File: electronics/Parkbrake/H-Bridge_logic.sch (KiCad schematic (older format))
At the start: 24 parts, among them U1 74LVC00, U2 74LVC08, U3 74LVC00, U4 74LVC08

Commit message: Spelling
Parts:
- U1, U3: farnell 2438786 -> 1105931; part 74LVC00APW.118 -> SN74LVC00APWR
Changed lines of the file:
@@
 F 2 "Housings_SSOP:TSSOP-14_4.4x5mm_Pitch0.65mm" H 1975 4775 50  0001 C CNN
 F 3 "" H 1975 4775 50  0000 C CNN
-F 4 "74LVC00APW.118" V 1975 4775 60  0001 C CNN "part"
-F 5 "2438786" V 1975 4775 60  0001 C CNN "farnell"
+F 4 "SN74LVC00APWR" V 1975 4775 60  0001 C CNN "part"
+F 5 "	1105931" V 1975 4775 60  0001 C CNN "farnell"
 	1    1975 4775
 	1    0    0    -1
@@
 F 2 "Housings_SSOP:TSSOP-14_4.4x5mm_Pitch0.65mm" H 6000 2025 50  0001 C CNN
 F 3 "" H 6000 2025 50  0000 C CNN
-F 4 "74LVC00APW.118" H 6000 2025 60  0001 C CNN "part"
-F 5 "2438786" H 6000 2025 60  0001 C CNN "farnell"
+F 4 "SN74LVC00APWR" H 6000 2025 60  0001 C CNN "part"
+F 5 "1105931" H 6000 2025 60  0001 C CNN "farnell"
 	1    6000 2025
 	1    0    0    -1

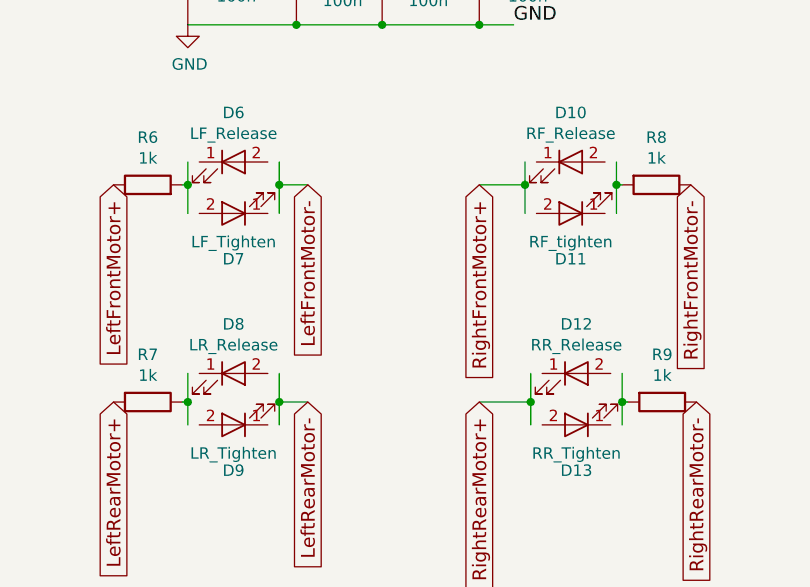
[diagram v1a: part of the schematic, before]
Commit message: minor tweaks to pcb, had a cap on wrong polarity
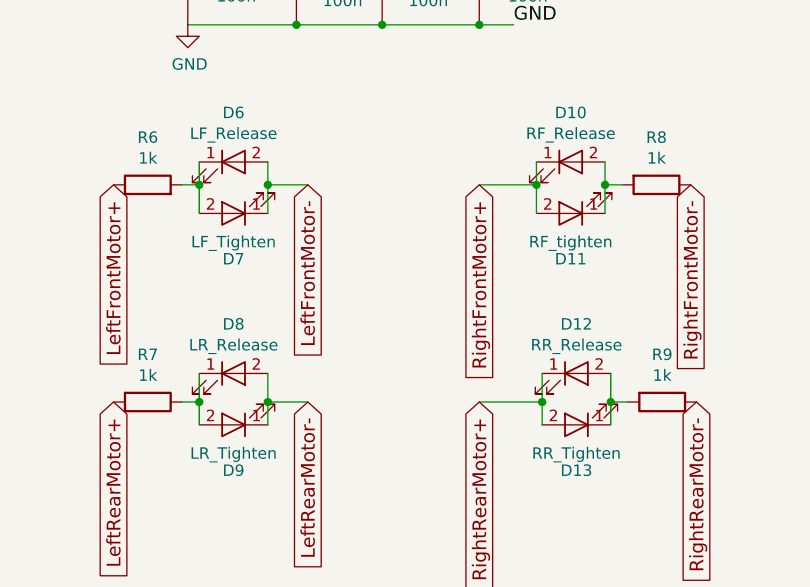
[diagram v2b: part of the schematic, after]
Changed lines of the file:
@@
 Connection ~ 2700 1200
-Wire Wire Line
-	3300 1800 3300 2025
-Wire Wire Line
-	3325 1900 3300 1900
-Connection ~ 3300 1900
-Wire Wire Line
-	2900 1800 2900 2025
-Wire Wire Line
-	2900 1900 2700 1900
-Connection ~ 2900 1900
-Wire Wire Line
-	1425 2725 1425 2950
-Wire Wire Line
-	1400 2850 1425 2850
-Connection ~ 1425 2850
-Wire Wire Line
-	1825 2725 1825 2950
-Wire Wire Line
-	1825 2850 1950 2850
-Connection ~ 1825 2850
-Wire Wire Line
-	1825 1800 1825 2025
-Wire Wire Line
-	1825 1900 1950 1900
-Connection ~ 1825 1900
-Wire Wire Line
-	1425 1800 1425 2025
-Wire Wire Line
-	1425 1900 1400 1900
-Connection ~ 1425 1900
-Wire Wire Line
-	3325 2725 3325 2950
-Wire Wire Line
-	3350 2850 3325 2850
-Connection ~ 3325 2850
-Wire Wire Line
-	2925 2725 2925 2950
-Wire Wire Line
-	2925 2850 2700 2850
-Connection ~ 2925 2850
 Wire Wire Line
 	2575 4775 2575 5175
@@
 	1    0    0    -1
 $EndComp
+Wire Wire Line
+	1775 1800 1775 2025
+Wire Wire Line
+	1475 1800 1475 2025
+Wire Wire Line
+	1400 1900 1475 1900
+Connection ~ 1475 1900
+Wire Wire Line
+	2950 1800 2950 2025
+Wire Wire Line
+	2700 1900 2950 1900
+Connection ~ 2950 1900
+Wire Wire Line
+	3250 1800 3250 2025
+Wire Wire Line
+	3325 1900 3250 1900
+Connection ~ 3250 1900
+Wire Wire Line
+	2975 2725 2975 2950
+Wire Wire Line
+	2700 2850 2975 2850
+Connection ~ 2975 2850
+Wire Wire Line
+	3275 2725 3275 2950
+Wire Wire Line
+	3350 2850 3275 2850
+Connection ~ 3275 2850
+Wire Wire Line
+	1475 2725 1475 2950
+Wire Wire Line
+	1400 2850 1475 2850
+Connection ~ 1475 2850
+Wire Wire Line
+	1775 2725 1775 2950
+Wire Wire Line
+	1950 2850 1775 2850
+Connection ~ 1775 2850
+Wire Wire Line
+	1950 1900 1775 1900
+Connection ~ 1775 1900
 $EndSCHEMATC

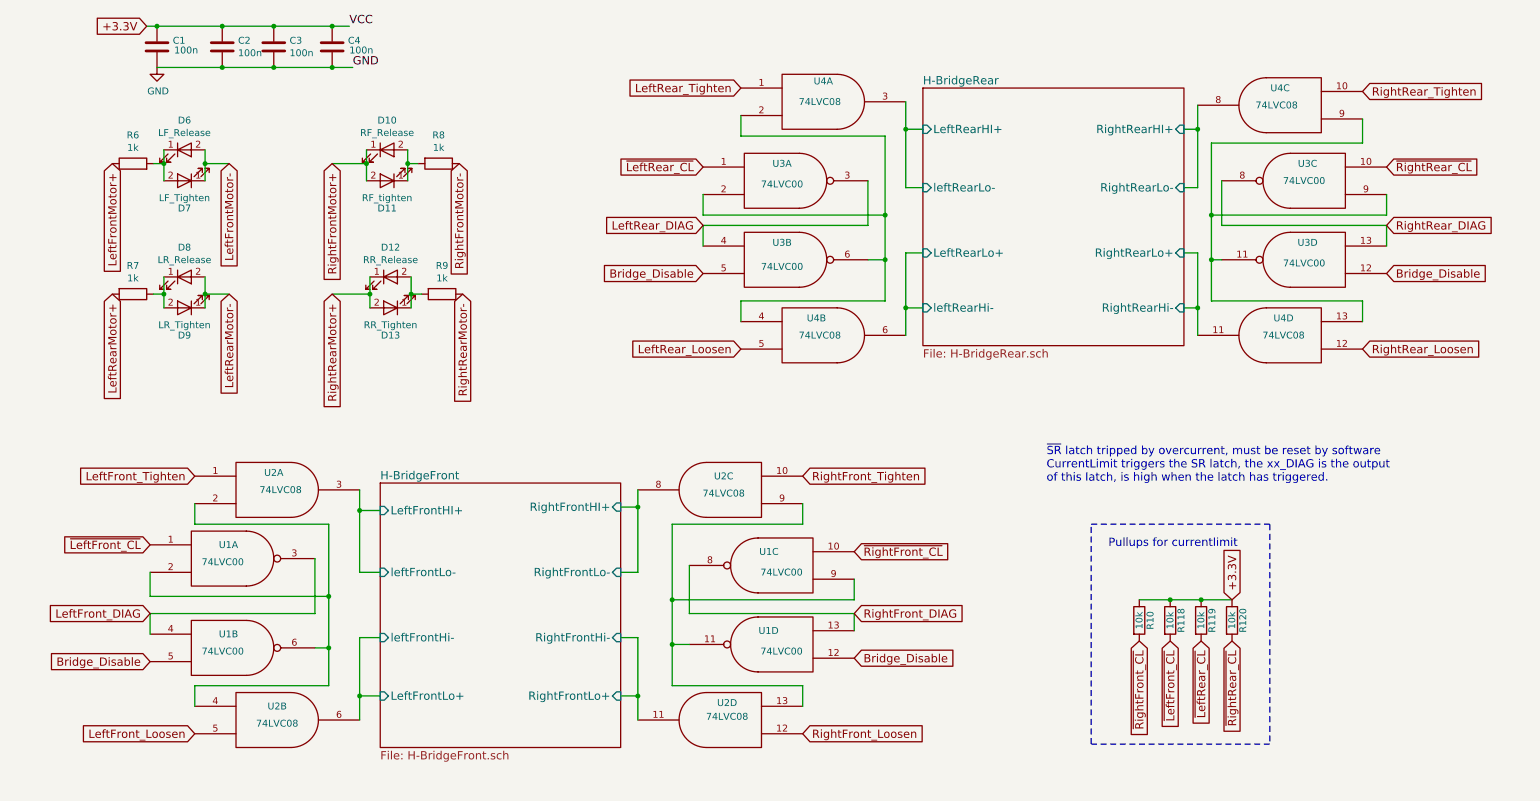
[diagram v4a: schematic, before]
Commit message: Rethink hardware current limit, it didn't work as I rememberd
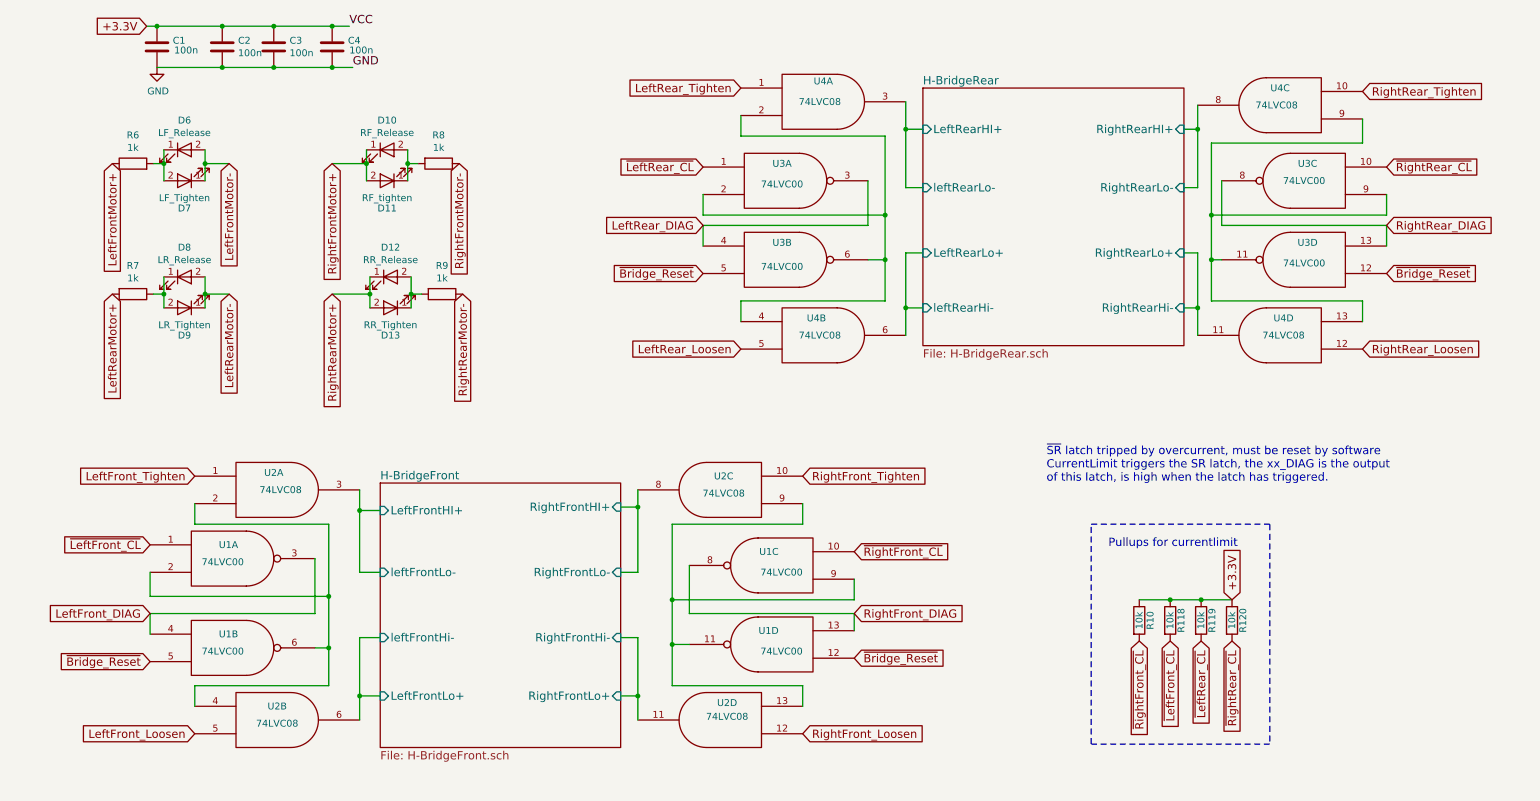
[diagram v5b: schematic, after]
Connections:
- net Bridge_Disable renamed ~Bridge_Reset
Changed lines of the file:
@@
 $EndComp
 Text GLabel 1375 5525 0    60   Input ~ 0
-Bridge_Disable
+~Bridge_Reset
 Text Notes 7900 4225 0    60   ~ 0
 ~SR~ latch tripped by overcurrent, must be reset by software\nCurrentLimit triggers the SR latch, the xx_DIAG is the output \nof this latch, is high when the latch has triggered.
@@
 Connection ~ 5175 5075
 Text GLabel 6500 5500 2    60   Input ~ 0
-Bridge_Disable
+~Bridge_Reset
 $Comp
 L 74LS08 U4
@@
 Connection ~ 6875 1650
 Text GLabel 5400 2700 0    60   Input ~ 0
-Bridge_Disable
+~Bridge_Reset
 Wire Wire Line
 	9175 2025 9175 2350
@@
 Connection ~ 9000 1650
 Text GLabel 10375 2700 2    60   Input ~ 0
-Bridge_Disable
+~Bridge_Reset
 Text GLabel 1375 5175 0    60   Input ~ 0
 LeftFront_DIAG
